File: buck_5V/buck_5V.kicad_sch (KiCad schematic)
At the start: 12 parts, among them J17 power, U18 MT2499A

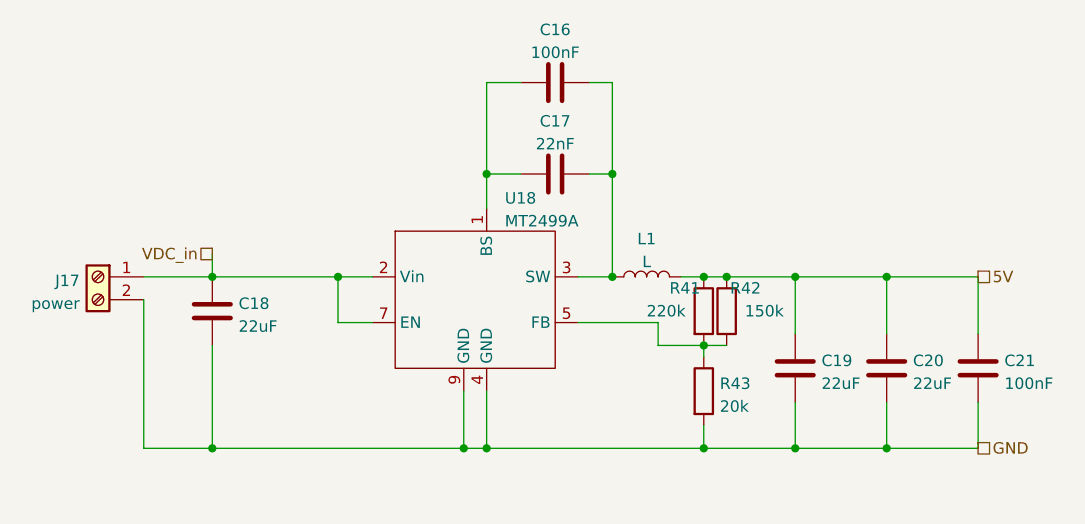
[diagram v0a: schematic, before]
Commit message: moved some schematic scheets to their own folders and routed a board with it. This allow for re-use of PCB parts.
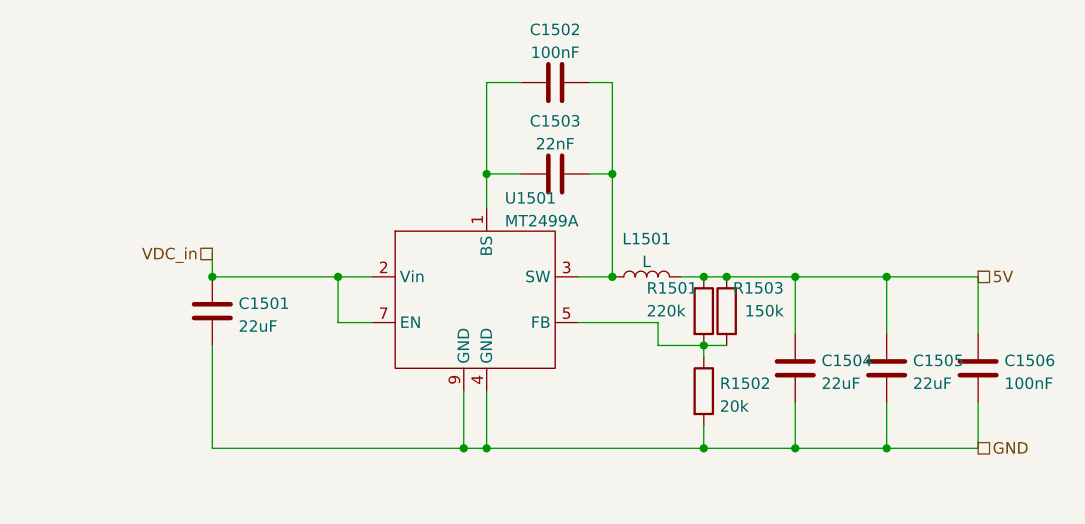
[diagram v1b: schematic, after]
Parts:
- removed J17: power, TerminalBlock_Phoenix:TerminalBlock_Phoenix_MKDS-1,5-2-5.08_1x02_P5.08mm_Horizontal, symbol Connector:Screw_Terminal_01x02
- C1501: renamed from C18; footprint Capacitor_SMD:C_0603_1608Metric_Pad1.08x0.95mm_HandSolder -> Capacitor_SMD:C_0603_1608Metric
- C1502: renamed from C16; footprint Capacitor_SMD:C_0402_1005Metric_Pad0.74x0.62mm_HandSolder -> Capacitor_SMD:C_0402_1005Metric
- C1503: renamed from C17; footprint Capacitor_SMD:C_0402_1005Metric_Pad0.74x0.62mm_HandSolder -> Capacitor_SMD:C_0402_1005Metric
- C1504: renamed from C19; footprint Capacitor_SMD:C_0603_1608Metric_Pad1.08x0.95mm_HandSolder -> Capacitor_SMD:C_0603_1608Metric
- C1505: renamed from C20; footprint Capacitor_SMD:C_0603_1608Metric_Pad1.08x0.95mm_HandSolder -> Capacitor_SMD:C_0603_1608Metric
- C1506: renamed from C21; footprint Capacitor_SMD:C_0402_1005Metric_Pad0.74x0.62mm_HandSolder -> Capacitor_SMD:C_0402_1005Metric
- R1501: renamed from R41; footprint Resistor_SMD:R_0603_1608Metric_Pad0.98x0.95mm_HandSolder -> Resistor_SMD:R_0603_1608Metric
- R1502: renamed from R43; footprint Resistor_SMD:R_0603_1608Metric_Pad0.98x0.95mm_HandSolder -> Resistor_SMD:R_0603_1608Metric
- R1503: renamed from R42; footprint Resistor_SMD:R_0603_1608Metric_Pad0.98x0.95mm_HandSolder -> Resistor_SMD:R_0603_1608Metric
- renumbered L1 to L1501, U18 to U1501

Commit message: changed incorrect LCSC numbers for the 5V buck converter. The inductor and a capacitor had wrong footprints. Also removed all fp-info-cache files
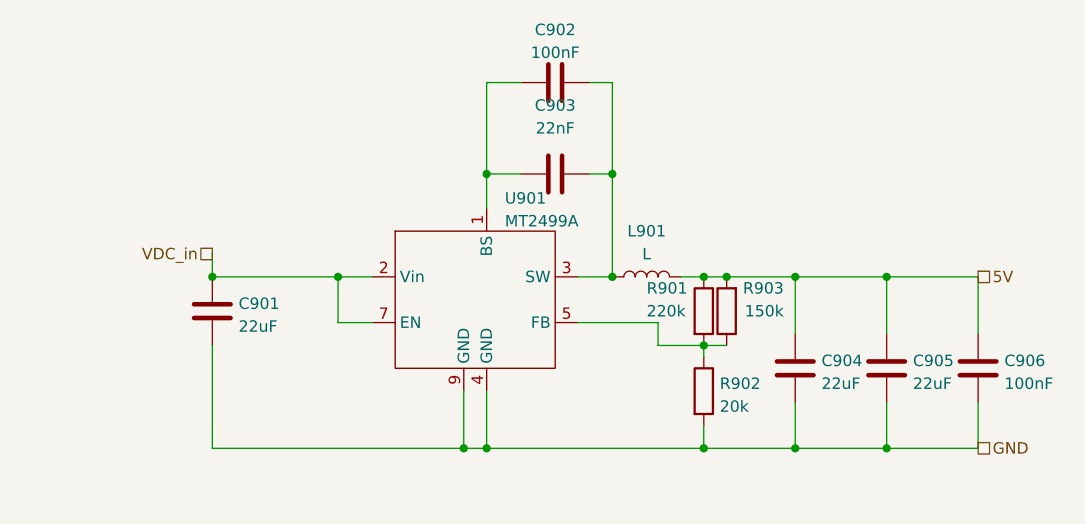
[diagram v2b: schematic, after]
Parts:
- removed C1503: 22nF, Capacitor_SMD:C_0402_1005Metric, symbol Device:C
- removed L1501: L, Inductor_SMD:L_Bourns-SRU8028_8.0x8.0mm, symbol Device:L
- added C903: 22nF, Capacitor_SMD:C_0402_1005Metric, symbol Device:C
- added L901: L, Inductor_SMD:L_Bourns-SRU8028_8.0x8.0mm, symbol Device:L
- renumbered C1501 to C901, C1502 to C902, C1504 to C904, C1505 to C905, C1506 to C906, R1501 to R901, R1502 to R902, R1503 to R903, U1501 to U901
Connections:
- net 5V: now also L901.2
- net at C902.1, U901.1 (BS): now also C903.1
- net at C902.2, U901.3 (SW): now also C903.2, L901.1
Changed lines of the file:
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@@
   (junction (at 158.75 74.93) (diameter 0) (color 0 0 0 0)
   )
+  (junction (at 156.21 82.55) (diameter 0) (color 0 0 0 0)
+  )
+  (junction (at 156.21 74.93) (diameter 0) (color 0 0 0 0)
+  )
+  (junction (at 129.54 93.98) (diameter 0) (color 0 0 0 0)
+  )
+  (junction (at 156.21 93.98) (diameter 0) (color 0 0 0 0)
+  )
   (junction (at 146.05 74.93) (diameter 0) (color 0 0 0 0)
-  )
-  (junction (at 156.21 82.55) (diameter 0) (color 0 0 0 0)
-  )
-  (junction (at 156.21 74.93) (diameter 0) (color 0 0 0 0)
-  )
-  (junction (at 129.54 93.98) (diameter 0) (color 0 0 0 0)
-  )
-  (junction (at 156.21 93.98) (diameter 0) (color 0 0 0 0)
   )
   (junction (at 146.05 63.5) (diameter 0) (color 0 0 0 0)
@@
     (effects (font (size 1.27 1.27)) (justify right))
   )
+  (symbol (lib_id "Device:C") (at 139.7 63.5 90) (unit 1)
+    (in_bom yes) (on_board yes) (dnp no) (fields_autoplaced)
+    (property "Reference" "C903" (at 139.7 55.88 90)
+      (effects (font (size 1.27 1.27)))
+    )
+    (property "Value" "22nF" (at 139.7 58.42 90)
+      (effects (font (size 1.27 1.27)))
+    )
+    (property "Footprint" "Capacitor_SMD:C_0402_1005Metric" (at 143.51 62.5348 0)
+      (effects (font (size 1.27 1.27)) hide)
+    )
+    (property "Datasheet" "~" (at 139.7 63.5 0)
+      (effects (font (size 1.27 1.27)) hide)
+    )
+    (property "JLCPCB Part#" "C1532" (at 139.7 63.5 90)
+      (effects (font (size 1.27 1.27)) hide)
+    )
+    (pin "1")
+    (pin "2")
+    (instances
+      (project "OS-servoDriver"
+        (path "/b6ccf16f-5cc5-4d5a-97fc-20f76ee5c73e/7745b34c-3ce1-4fee-9e05-e2cc7dc8f5e5"
+          (reference "C903") (unit 1)
+        )
+      )
+      (project "buck_5V"
+        (path "/d1cb43a0-bc81-49bf-86a7-735d10d531df"
+          (reference "C903") (unit 1)
+        )
+      )
+      (project "general_schematics"
+        (path "/e777d9ec-d073-4229-a9e6-2cf85636e407/891f98c0-3628-49fd-a4d5-1cf0156a22a0"
+          (reference "C1503") (unit 1)
+        )
+      )
+    )
+  )
   (symbol (lib_id "Device:R") (at 158.75 78.74 180) (unit 1)
     (in_bom yes) (on_board yes) (dnp no)
-    (property "Reference" "R1503" (at 165.1 76.2 0)
+    (property "Reference" "R903" (at 165.1 76.2 0)
       (effects (font (size 1.27 1.27)) (justify left))
     )
@@
   (symbol (lib_id "Device:C") (at 139.7 53.34 90) (unit 1)
     (in_bom yes) (on_board yes) (dnp no) (fields_autoplaced)
-    (property "Reference" "C1502" (at 139.7 47.4812 90)
+    (property "Reference" "C902" (at 139.7 47.4812 90)
       (effects (font (size 1.27 1.27)))
     )
@@
     )
   )
-  (symbol (lib_id "Device:C") (at 139.7 63.5 90) (unit 1)
-    (in_bom yes) (on_board yes) (dnp no) (fields_autoplaced)
-    (property "Reference" "C1503" (at 139.7 57.6412 90)
-      (effects (font (size 1.27 1.27)))
-    )
-    (property "Value" "22nF" (at 139.7 60.1781 90)
-      (effects (font (size 1.27 1.27)))
-    )
-    (property "Footprint" "Capacitor_SMD:C_0402_1005Metric" (at 143.51 62.5348 0)
-      (effects (font (size 1.27 1.27)) hide)
-    )
-    (property "Datasheet" "~" (at 139.7 63.5 0)
-      (effects (font (size 1.27 1.27)) hide)
-    )
-    (property "JLCPCB Part#" "C1729" (at 139.7 63.5 90)
-      (effects (font (size 1.27 1.27)) hide)
-    )
-    (pin "1")
-    (pin "2")
-    (instances
-      (project "buck_5V"
-        (path "/d1cb43a0-bc81-49bf-86a7-735d10d531df"
-          (reference "C903") (unit 1)
-        )
-      )
-      (project "general_schematics"
-        (path "/e777d9ec-d073-4229-a9e6-2cf85636e407/891f98c0-3628-49fd-a4d5-1cf0156a22a0"
-          (reference "C1503") (unit 1)
-        )
-      )
-    )
-  )
   (symbol (lib_id "Device:L") (at 149.86 74.93 90) (unit 1)
     (in_bom yes) (on_board yes) (dnp no) (fields_autoplaced)
-    (property "Reference" "L1501" (at 149.86 70.7222 90)
-      (effects (font (size 1.27 1.27)))
-    )
-    (property "Value" "L" (at 149.86 73.2591 90)
+    (property "Reference" "L901" (at 149.86 69.85 90)
+      (effects (font (size 1.27 1.27)))
+    )
+    (property "Value" "L" (at 149.86 72.39 90)
       (effects (font (size 1.27 1.27)))
     )
@@
       (effects (font (size 1.27 1.27)) hide)
     )
-    (property "JLCPCB Part#" "C2929438" (at 149.86 74.93 90)
-      (effects (font (size 1.27 1.27)) hide)
-    )
-    (pin "1")
-    (pin "2")
-    (instances
-      (project "buck_5V"
-        (path "/d1cb43a0-bc81-49bf-86a7-735d10d531df"
+    (property "JLCPCB Part#" "C92945" (at 149.86 74.93 90)
+      (effects (font (size 1.27 1.27)) hide)
+    )
+    (pin "1")
+    (pin "2")
+    (instances
+      (project "OS-servoDriver"
+        (path "/b6ccf16f-5cc5-4d5a-97fc-20f76ee5c73e/7745b34c-3ce1-4fee-9e05-e2cc7dc8f5e5"
           (reference "L901") (unit 1)
         )
       )
+      (project "buck_5V"
+        (path "/d1cb43a0-bc81-49bf-86a7-735d10d531df"
+          (reference "L901") (unit 1)
+        )
+      )
       (project "general_schematics"
         (path "/e777d9ec-d073-4229-a9e6-2cf85636e407/891f98c0-3628-49fd-a4d5-1cf0156a22a0"
@@
   (symbol (lib_id "Device:C") (at 176.53 85.09 0) (unit 1)
     (in_bom yes) (on_board yes) (dnp no) (fields_autoplaced)
-    (property "Reference" "C1505" (at 179.451 84.2553 0)
+    (property "Reference" "C905" (at 179.451 84.2553 0)
       (effects (font (size 1.27 1.27)) (justify left))
     )
@@
   (symbol (lib_id "Device:C") (at 101.6 78.74 0) (unit 1)
     (in_bom yes) (on_board yes) (dnp no) (fields_autoplaced)
-    (property "Reference" "C1501" (at 104.521 77.9053 0)
+    (property "Reference" "C901" (at 104.521 77.9053 0)
       (effects (font (size 1.27 1.27)) (justify left))
     )
@@
   (symbol (lib_id "Device:R") (at 156.21 87.63 0) (unit 1)
     (in_bom yes) (on_board yes) (dnp no)
-    (property "Reference" "R1502" (at 157.988 86.7953 0)
+    (property "Reference" "R902" (at 157.988 86.7953 0)
       (effects (font (size 1.27 1.27)) (justify left))
     )
@@
   (symbol (lib_id "custom_kicad_lib_sk:MT499A") (at 132.08 76.2 0) (unit 1)
     (in_bom yes) (on_board yes) (dnp no) (fields_autoplaced)
-    (property "Reference" "U1501" (at 134.0994 66.201 0)
+    (property "Reference" "U901" (at 134.0994 66.201 0)
       (effects (font (size 1.27 1.27)) (justify left))
     )
@@
   (symbol (lib_id "Device:C") (at 166.37 85.09 0) (unit 1)
     (in_bom yes) (on_board yes) (dnp no) (fields_autoplaced)
-    (property "Reference" "C1504" (at 169.291 84.2553 0)
+    (property "Reference" "C904" (at 169.291 84.2553 0)
       (effects (font (size 1.27 1.27)) (justify left))
     )
@@
   (symbol (lib_id "Device:R") (at 156.21 78.74 0) (unit 1)
     (in_bom yes) (on_board yes) (dnp no)
-    (property "Reference" "R1501" (at 149.86 76.2 0)
+    (property "Reference" "R901" (at 149.86 76.2 0)
       (effects (font (size 1.27 1.27)) (justify left))
     )
@@
   (symbol (lib_id "Device:C") (at 186.69 85.09 0) (unit 1)
     (in_bom yes) (on_board yes) (dnp no) (fields_autoplaced)
-    (property "Reference" "C1506" (at 189.611 84.2553 0)
-      (effects (font (size 1.27 1.27)) (justify left))
-    )
+    (property "Reference" "C906" (at 189.611 84.2553 0)
+      (effects (font (size 1.27 1.27)) (justify left))
+    )

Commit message: removed hierarchial labels for power symbols and replaced them with actual power symbols also updated footprint of the inductor of the 5V buck
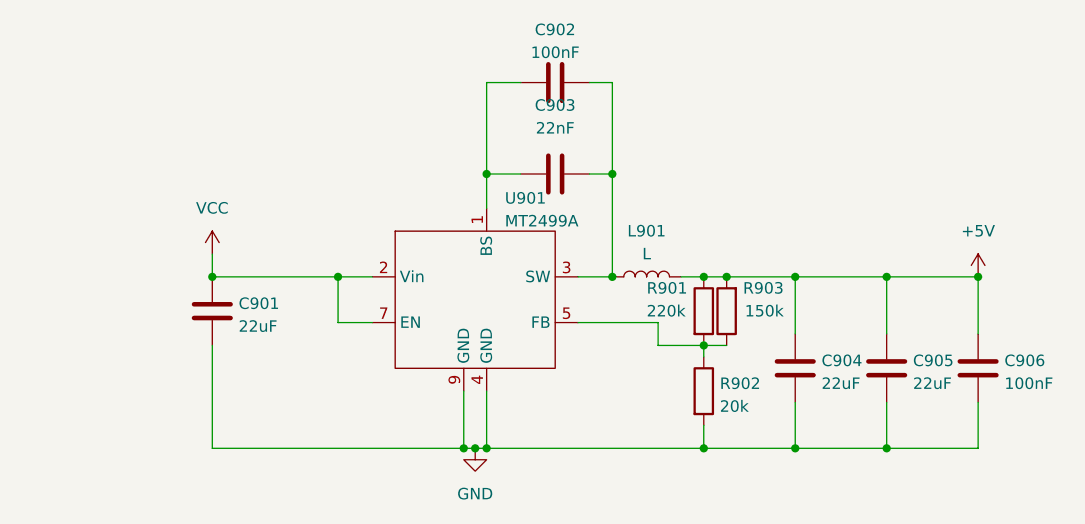
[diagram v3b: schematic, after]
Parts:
- L901: footprint Inductor_SMD:L_Bourns-SRU8028_8.0x8.0mm -> Inductor_SMD:L_Bourns-SRN8040_8x8.15mm
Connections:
- net 5V renamed +5V
- net VDC_in renamed VCC
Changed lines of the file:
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@@
   (junction (at 115.57 74.93) (diameter 0) (color 0 0 0 0)
   )
+  (junction (at 130.81 93.98) (diameter 0) (color 0 0 0 0)
+  )
   (junction (at 158.75 74.93) (diameter 0) (color 0 0 0 0)
   )
@@
   (junction (at 132.08 63.5) (diameter 0) (color 0 0 0 0)
   )
+  (junction (at 186.69 74.93) (diameter 0) (color 0 0 0 0)
+  )
   (junction (at 132.08 93.98) (diameter 0) (color 0 0 0 0)
   )
@@
     (stroke (width 0) (type default))
   )
-  (wire (pts (xy 132.08 93.98) (xy 129.54 93.98))
+  (wire (pts (xy 132.08 93.98) (xy 130.81 93.98))
     (stroke (width 0) (type default))
   )
@@
     (stroke (width 0) (type default))
   )
+  (wire (pts (xy 130.81 93.98) (xy 129.54 93.98))
+    (stroke (width 0) (type default))
+  )
   (wire (pts (xy 119.38 80.01) (xy 115.57 80.01))
     (stroke (width 0) (type default))
@@
   (wire (pts (xy 142.24 80.01) (xy 151.13 80.01))
     (stroke (width 0) (type default))
-  )
-  (hierarchical_label "5V" (shape passive) (at 186.69 74.93 0) (fields_autoplaced)
-    (effects (font (size 1.27 1.27)) (justify left))
-  )
-  (hierarchical_label "GND" (shape passive) (at 186.69 93.98 0) (fields_autoplaced)
-    (effects (font (size 1.27 1.27)) (justify left))
-  )
-  (hierarchical_label "VDC_in" (shape passive) (at 101.6 72.39 180) (fields_autoplaced)
-    (effects (font (size 1.27 1.27)) (justify right))
   )
   (symbol (lib_id "Device:C") (at 139.7 63.5 90) (unit 1)
@@
       (effects (font (size 1.27 1.27)))
     )
-    (property "Footprint" "Inductor_SMD:L_Bourns-SRU8028_8.0x8.0mm" (at 149.86 74.93 0)
+    (property "Footprint" "Inductor_SMD:L_Bourns-SRN8040_8x8.15mm" (at 149.86 74.93 0)
       (effects (font (size 1.27 1.27)) hide)
     )
@@
         (path "/e777d9ec-d073-4229-a9e6-2cf85636e407/891f98c0-3628-49fd-a4d5-1cf0156a22a0"
           (reference "R1502") (unit 1)
+        )
+      )
+    )
+  )
+  (symbol (lib_id "power:GND") (at 130.81 93.98 0) (unit 1)
+    (in_bom yes) (on_board yes) (dnp no) (fields_autoplaced)
+    (property "Reference" "#PWR0903" (at 130.81 100.33 0)
+      (effects (font (size 1.27 1.27)) hide)
+    )
+    (property "Value" "GND" (at 130.81 99.06 0)
+      (effects (font (size 1.27 1.27)))
+    )
+    (property "Footprint" "" (at 130.81 93.98 0)
+      (effects (font (size 1.27 1.27)) hide)
+    )
+    (property "Datasheet" "" (at 130.81 93.98 0)
+      (effects (font (size 1.27 1.27)) hide)
+    )
+    (pin "1")
+    (instances
+      (project "buck_5V"
+        (path "/d1cb43a0-bc81-49bf-86a7-735d10d531df"
+          (reference "#PWR0903") (unit 1)
+        )
+      )
+    )
+  )
+  (symbol (lib_id "power:+5V") (at 186.69 74.93 0) (unit 1)
+    (in_bom yes) (on_board yes) (dnp no) (fields_autoplaced)
+    (property "Reference" "#PWR0902" (at 186.69 78.74 0)
+      (effects (font (size 1.27 1.27)) hide)
+    )
+    (property "Value" "+5V" (at 186.69 69.85 0)
+      (effects (font (size 1.27 1.27)))
+    )
+    (property "Footprint" "" (at 186.69 74.93 0)
+      (effects (font (size 1.27 1.27)) hide)
+    )
+    (property "Datasheet" "" (at 186.69 74.93 0)
+      (effects (font (size 1.27 1.27)) hide)
+    )
+    (pin "1")
+    (instances
+      (project "buck_5V"
+        (path "/d1cb43a0-bc81-49bf-86a7-735d10d531df"
+          (reference "#PWR0902") (unit 1)
         )
       )
@@
         )
       )
+    )
+  )
+  (symbol (lib_id "power:VCC") (at 101.6 72.39 0) (unit 1)
+    (in_bom yes) (on_board yes) (dnp no) (fields_autoplaced)
+    (property "Reference" "#PWR0901" (at 101.6 76.2 0)
+      (effects (font (size 1.27 1.27)) hide)
+    )
+    (property "Value" "VCC" (at 101.6 67.31 0)
+      (effects (font (size 1.27 1.27)))
+    )
+    (property "Footprint" "" (at 101.6 72.39 0)
+      (effects (font (size 1.27 1.27)) hide)
+    )
+    (property "Datasheet" "" (at 101.6 72.39 0)
+      (effects (font (size 1.27 1.27)) hide)
+    )
+    (pin "1")
+    (instances
+      (project "buck_5V"
+        (path "/d1cb43a0-bc81-49bf-86a7-735d10d531df"
+          (reference "#PWR0901") (unit 1)
+        )
+      )
